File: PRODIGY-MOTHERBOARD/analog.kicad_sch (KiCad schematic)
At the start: 24 parts, among them Q6 ALS-PDIC15-21B/TR8, U26 NJM5532

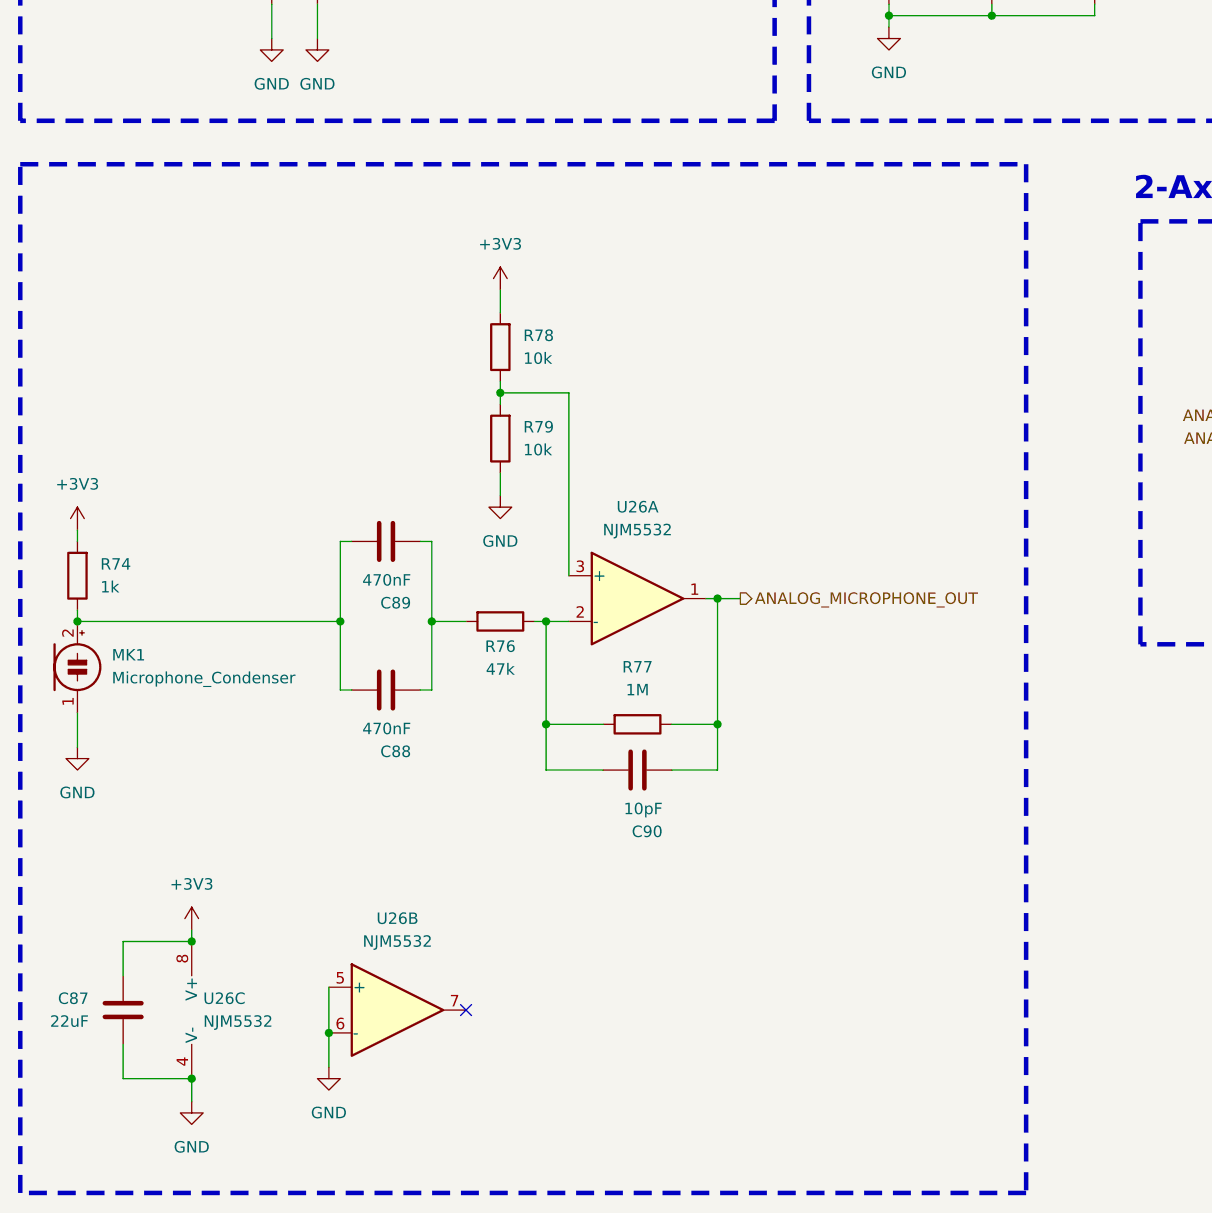
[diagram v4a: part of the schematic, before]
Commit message: Added pins to MCU. Added Decoder for SPI SS-Multiplexing.
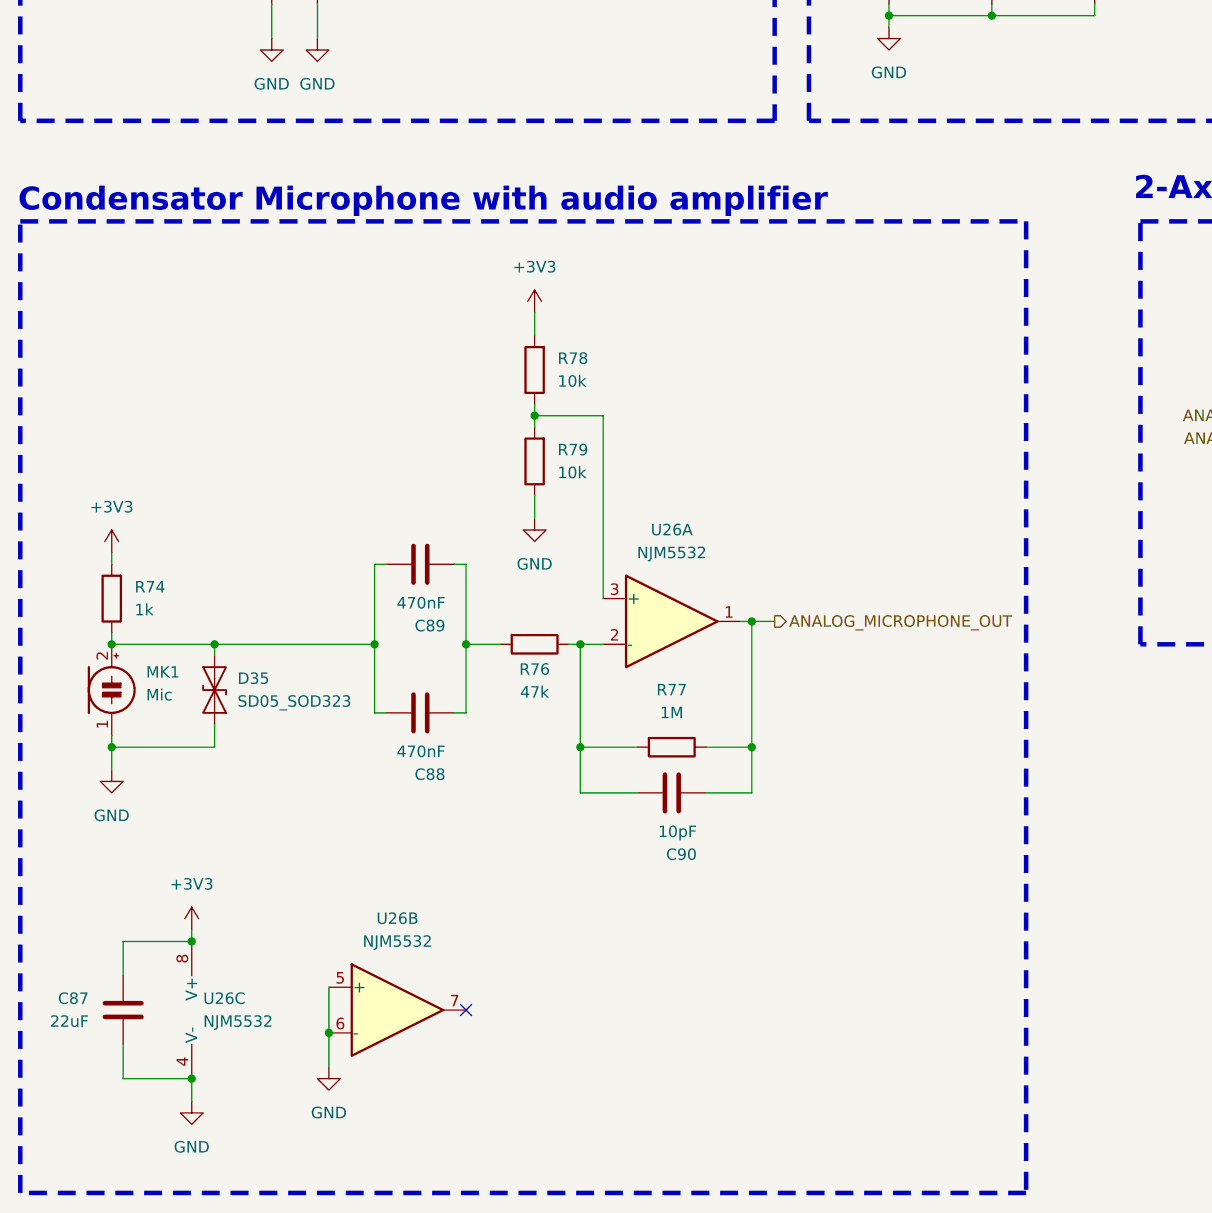
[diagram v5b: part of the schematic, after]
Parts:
- added D35: SD05_SOD323, Diode_SMD:D_SOD-323, symbol Diode:SD05_SOD323
- MK1: value Microphone_Condenser -> Mic; footprint Buzzer_Beeper:MagneticBuzzer_Kingstate_KCG0601 -> Sensor_Audio:POM-2244P-C3310-2-R
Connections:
- net GND: now also D35.1 (A1)
- net at C88.1, C89.1, MK1.2 (+)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: now also D35.2 (A2)
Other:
- note added: "Condensator Microphone with audio amplifier"
- moved on the sheet: C88, C89, C90, MK1, R74, R76, R77, R78, R79, U26A

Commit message: Added proper debounce filter elements to buttons.
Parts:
- renumbered C85 to C83, C89 to C84, C88 to C85, C90 to C86, D11 to D43, D10 to D44, D31 to D45, D32 to D46, D33 to D47, D34 to D48, D35 to D49, R69 to R73, R75 to R74, R78 to R75, R79 to R76, R74 to R77, R76 to R78, R77 to R79, U26 to U25
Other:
- moved on the sheet: D47, D48, RV4

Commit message: Submitted V0 for evaluation. Avaiting feedback.
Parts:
- renumbered D43 to D62, D44 to D63, D45 to D64, D46 to D65, D47 to D66, D48 to D67, D49 to D68, R73 to R74, R74 to R75, R75 to R76, R76 to R77, R77 to R78, R78 to R79, R79 to R80, U25 to U26

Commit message: Finished v0.1 schematic.
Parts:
- renumbered C87 to C80, C84 to C81, C85 to C82, C86 to C83, C83 to C84, D68 to D65, D62 to D66, D63 to D67, D64 to D68, D66 to D69, D67 to D70, D65 to D71, R78 to R65, R76 to R66, R77 to R67, R79 to R68, R80 to R69, R74 to R70, R75 to R71, RV3 to RV2, RV4 to RV3, U26 to U21
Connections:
- net +3V3 renamed +3.3VA
